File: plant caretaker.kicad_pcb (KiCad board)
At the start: 2 copper layers, 56 parts, among them J3 Water_Pump, J4 Kitronik, J5 694106402002, Q1 FDMS86255, U1 UDA1380HN_N2, U2 TMP175AIDR, U4 LM2596S-5, U5 PAM8403D, U6 ESP32_C3_ZERO

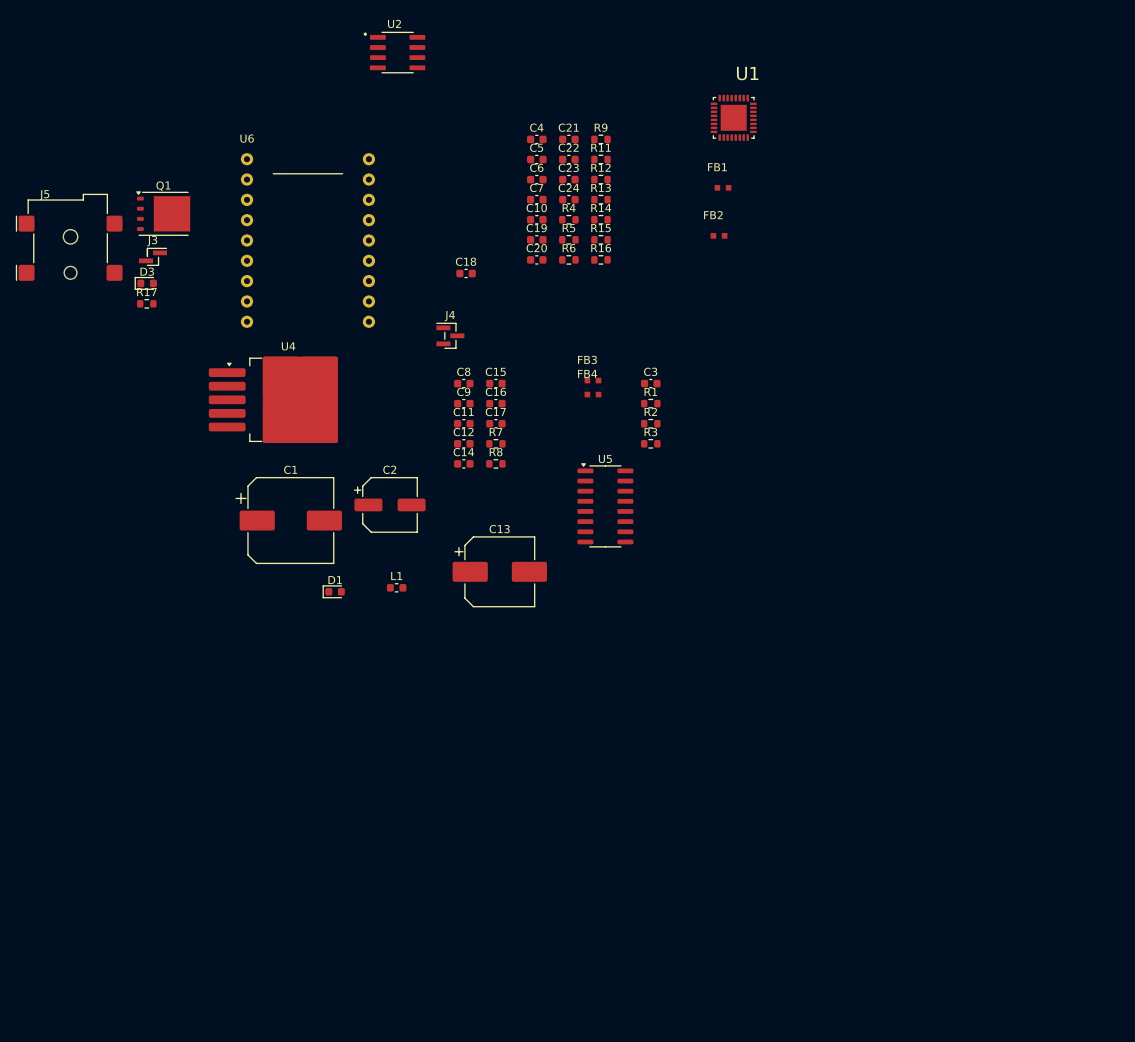
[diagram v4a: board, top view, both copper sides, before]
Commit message: Started power connections
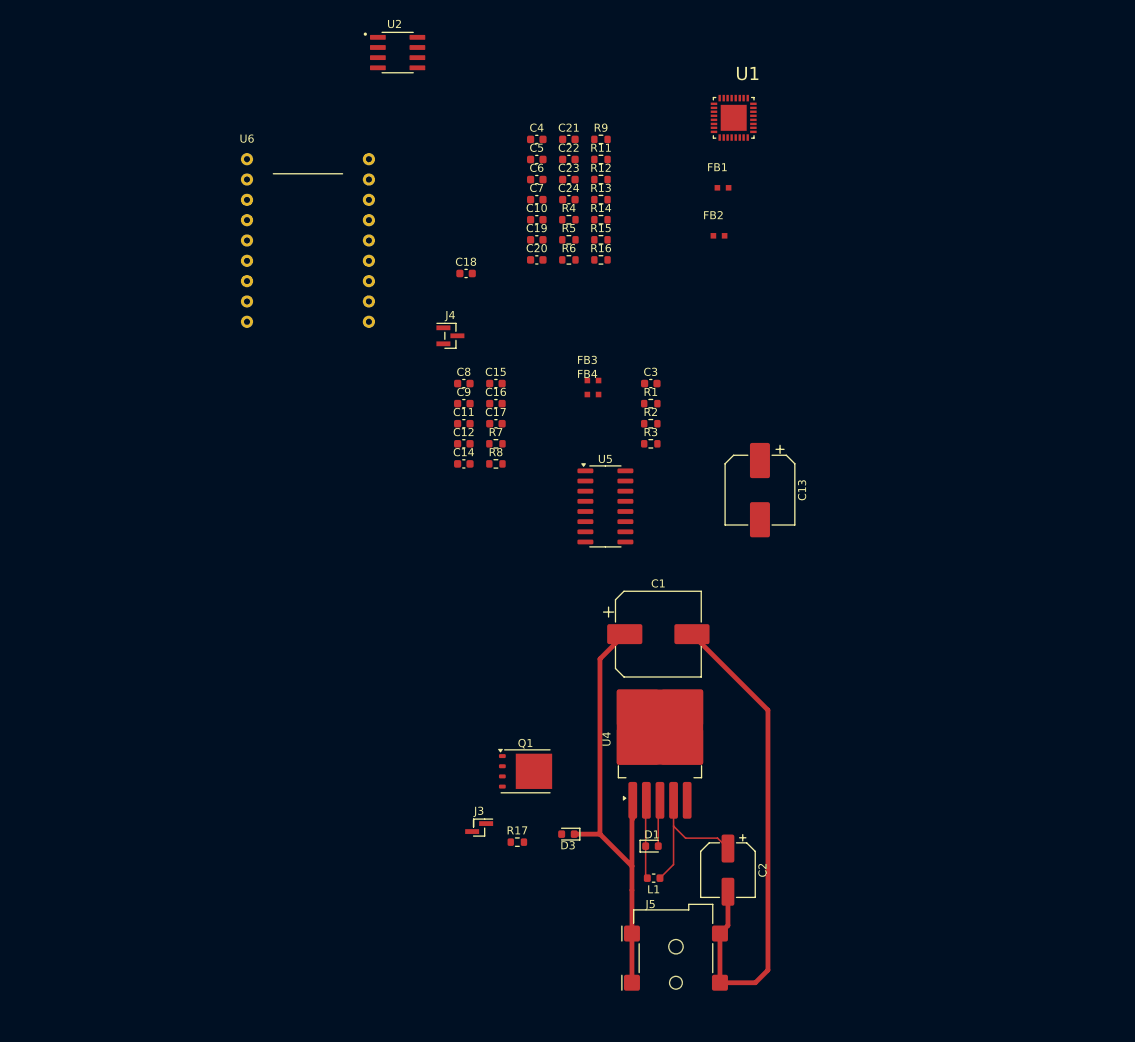
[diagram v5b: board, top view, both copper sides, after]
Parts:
- moved J5 116.6 mm to (118.0, 133.0)
- moved D3 86.6 mm to (104.5, 117.5), turned to 180 degrees
- moved Q1 83.1 mm to (99.2, 109.7)
- moved J3 82.2 mm to (93.4, 116.7)
- moved R17 81.7 mm to (98.2, 118.5)
- moved U4 62.9 mm to (116.0, 105.6), turned to 90 degrees
- moved C2 62.2 mm to (124.5, 122.0), turned to -90 degrees
- moved D1 50.8 mm to (115.0, 119.0)
- moved L1 48.5 mm to (115.2, 123.0), turned to 180 degrees
- moved C1 48.1 mm to (115.8, 92.5)
- moved C13 34.1 mm to (128.5, 74.5), turned to -90 degrees
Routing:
- net GND: track 0.00 -> 70.2 mm
- net Net-(D3-K): track 0.00 -> 60.3 mm
- net /BuckConverter/5V_OUT: track 0.00 -> 18.4 mm
- net Net-(D1-K): track 0.00 -> 9.85 mm

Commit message: Added power polygon and edge cuts
Also added 12V label to schematic for polygon net class
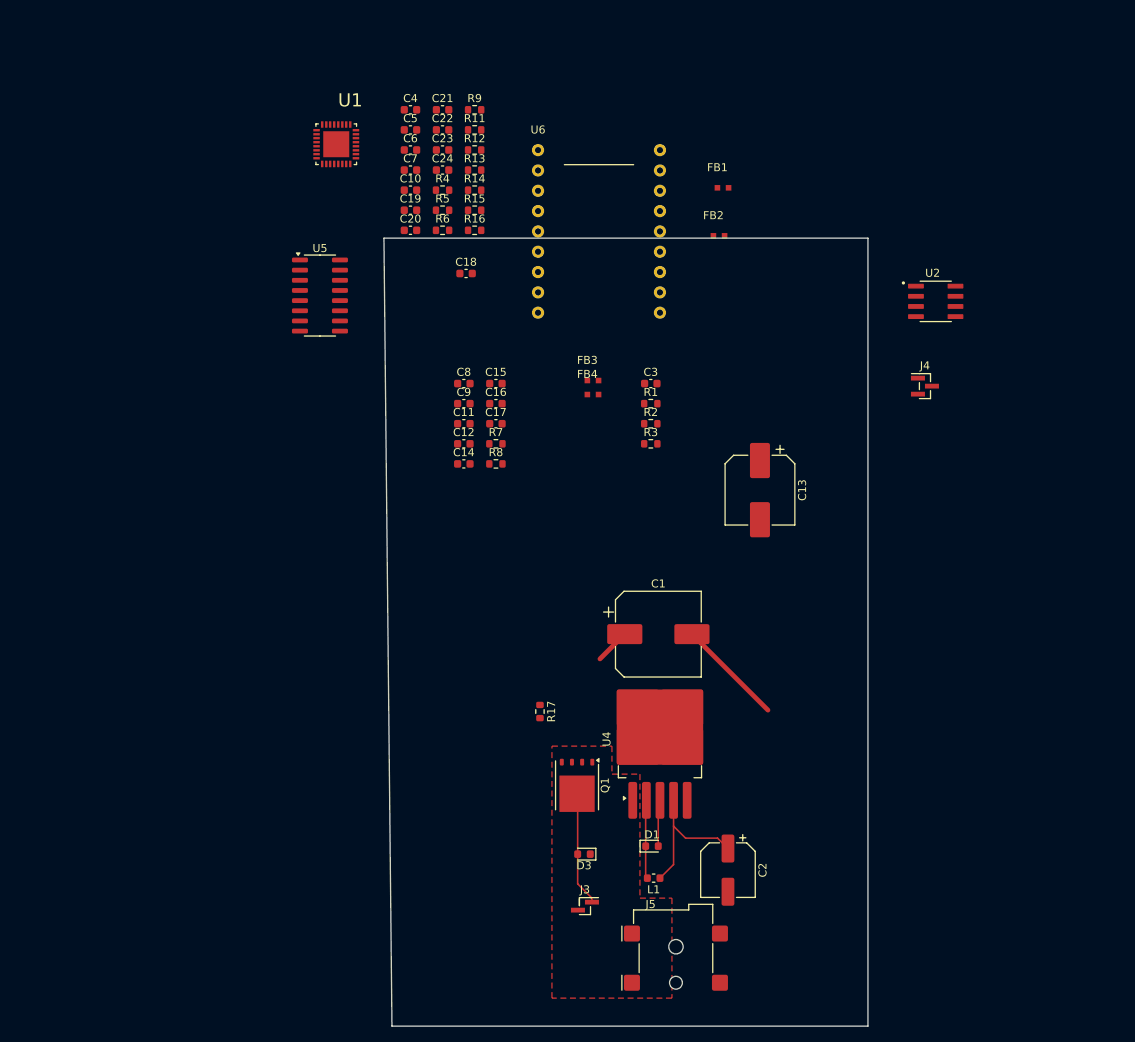
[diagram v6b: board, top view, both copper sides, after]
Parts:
- moved U2 74.1 mm to (150.5, 50.9)
- moved J4 59.7 mm to (149.1, 61.5)
- moved U1 49.8 mm to (75.5, 31.3)
- moved U5 44.4 mm to (73.5, 50.2)
- moved U6 36.4 mm to (100.8, 32.0)
- moved R17 16.6 mm to (101.0, 102.2), turned to -90 degrees
- moved J3 16.5 mm to (106.6, 126.5)
- moved C10 16.2 mm to (84.8, 37.0)
- moved C19 16.2 mm to (84.8, 39.5)
- moved C20 16.2 mm to (84.8, 42.0)
- moved C4 16.2 mm to (84.8, 27.0)
- moved C5 16.2 mm to (84.8, 29.5)
- moved C6 16.2 mm to (84.8, 32.0)
- moved C7 16.2 mm to (84.8, 34.5)
- moved R11 16.2 mm to (92.8, 29.5)
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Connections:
- net Net-(D3-K) renamed /BuckConverter/12V
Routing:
- net /BuckConverter/12V: track 60.3 -> 4.38 mm
- net GND: track 70.2 -> 19.2 mm
- net Net-(D3-A): track 0.00 -> 14.3 mm
- added copper zone on F.Cu, net /BuckConverter/12V
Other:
- board outline added: 60.5 x 98.5 mm

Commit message: PCB - power connected
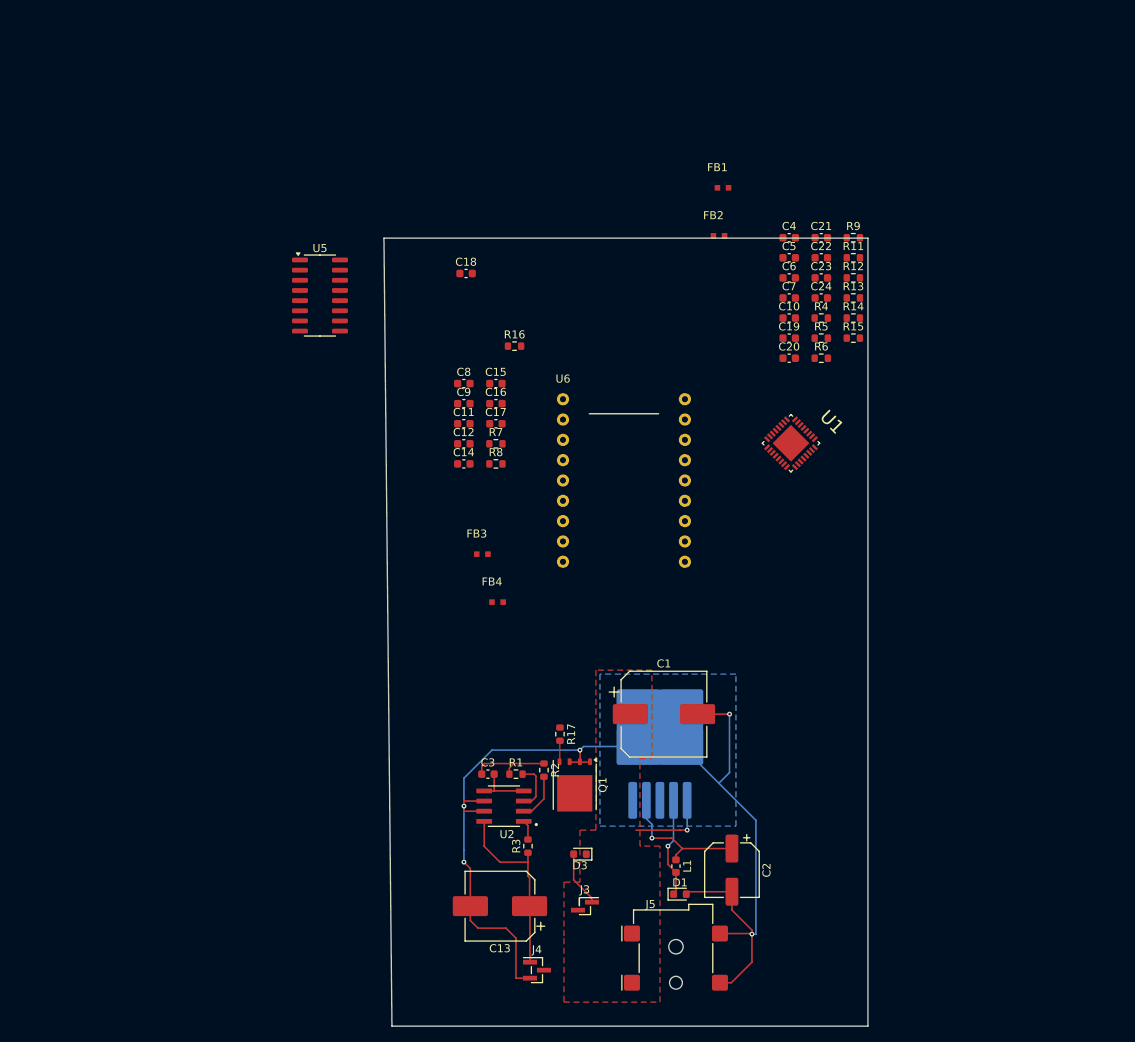
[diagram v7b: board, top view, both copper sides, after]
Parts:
- U4: moved to B.Cu
- moved J4 87.6 mm to (100.6, 134.5)
- moved U2 83.0 mm to (96.5, 114.0), turned to 180 degrees
- moved U1 68.0 mm to (132.4, 68.6), turned to -45 degrees
- moved C13 61.3 mm to (96.0, 126.5), turned to 180 degrees
- moved C3 52.9 mm to (94.5, 110.0)
- moved R3 52.6 mm to (99.5, 119.0), turned to 90 degrees
- moved R11 50.0 mm to (140.2, 45.5)
- moved R12 50.0 mm to (140.2, 48.0)
- moved R13 50.0 mm to (140.2, 50.5)
- moved R14 50.0 mm to (140.2, 53.0)
- moved R15 50.0 mm to (140.2, 55.5)
- moved R9 50.0 mm to (140.2, 43.0)
- moved C10 50.0 mm to (132.2, 53.0)
- moved C19 50.0 mm to (132.2, 55.5)
- moved C20 50.0 mm to (132.2, 58.0)
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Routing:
- net GND: track 19.2 -> 138.0 mm, vias 0 -> 5
- net +3V3: track 0.00 -> 33.7 mm
- net Net-(D3-A): track 14.3 -> 6.95 mm
- net /TempSensor/ALERT: track 0.00 -> 6.10 mm
- net /AudioCodec/SCL: track 0.00 -> 5.93 mm
- net /BuckConverter/12V: track 4.38 -> 10.2 mm, vias 0 -> 1
- net Net-(D1-K): track 9.85 -> 12.5 mm, vias 0 -> 1
- net Net-(Q1-G): track 0.00 -> 2.68 mm
- net /AudioCodec/SDA: track 0.00 -> 2.49 mm
- net /BuckConverter/5V_OUT: track 18.4 -> 16.8 mm, vias 0 -> 1
- added copper zone on B.Cu, net GND

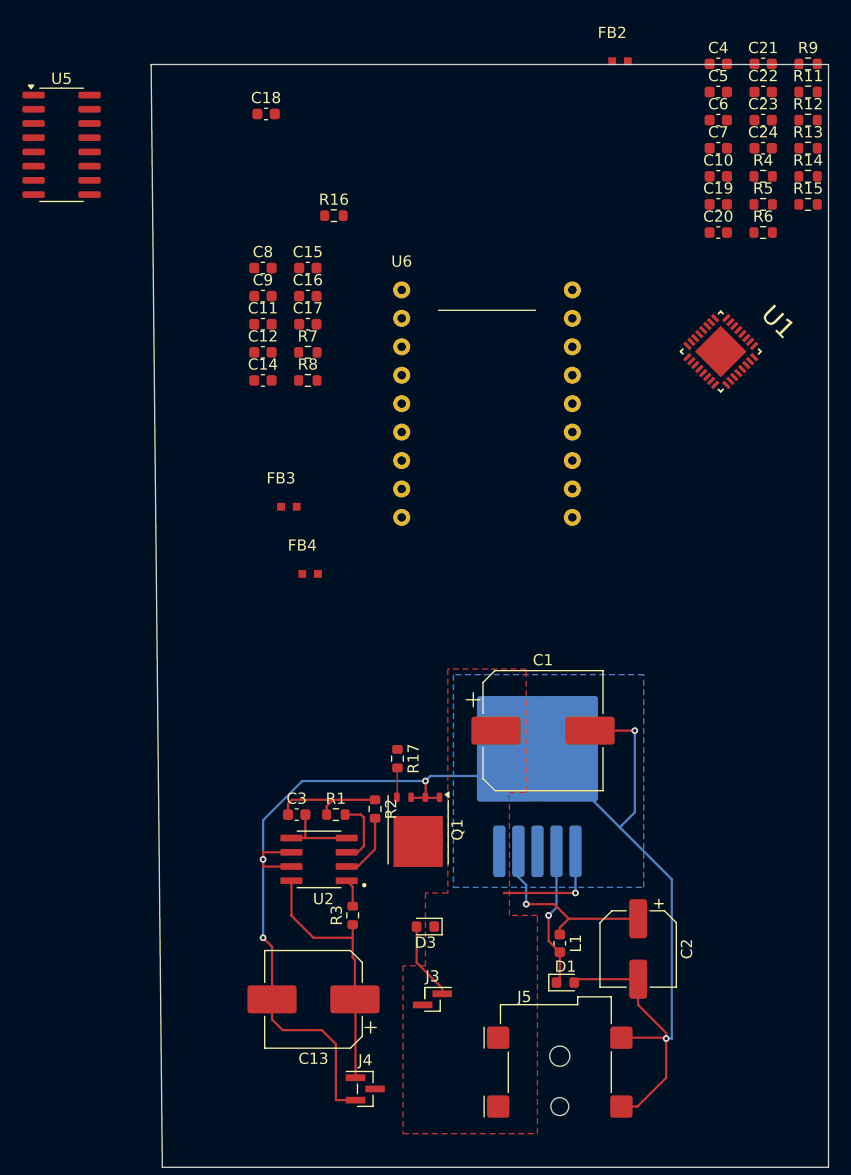
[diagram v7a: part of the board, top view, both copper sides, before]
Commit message: Fixed ESP32 library
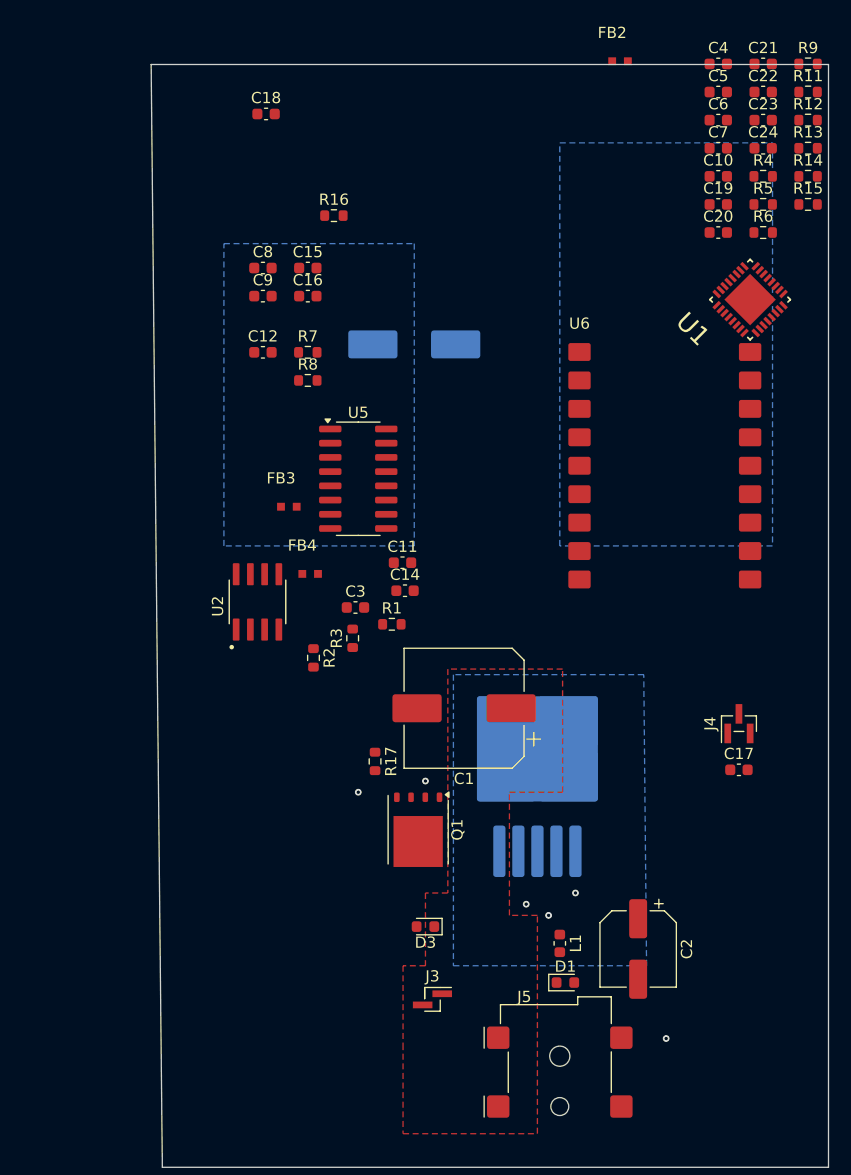
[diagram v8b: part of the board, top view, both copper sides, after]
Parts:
- C13: moved to B.Cu
- U6: footprint ESP32_C3_ZERO_Library:ESP32_C3_ZERO -> ESP32_C3_Zero:ESP32_C3_ZERO
- moved C13 59.2 mm to (105.0, 68.0)
- moved C17 55.4 mm to (134.0, 106.0)
- moved J4 46.7 mm to (134.0, 101.9), turned to 90 degrees
- moved U5 39.9 mm to (100.0, 80.0)
- moved R3 24.8 mm to (99.5, 94.2)
- moved C11 24.7 mm to (104.0, 87.5)
- moved U2 23.6 mm to (91.0, 91.0), turned to 90 degrees
- moved C14 22.7 mm to (104.2, 90.0)
- moved C3 19.2 mm to (99.8, 91.5)
- moved R1 17.7 mm to (103.0, 93.0)
- moved U6 16.8 mm to (119.8, 68.7)
- moved R2 14.6 mm to (96.0, 96.0)
- moved C1 7.33 mm to (109.5, 100.5), turned to 180 degrees
- moved U1 5.33 mm to (135.0, 64.0), turned to 135 degrees
- moved R17 2.02 mm to (101.5, 105.2)
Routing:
- net GND: track 138.0 -> 0.13 mm, vias 5 -> 3
- net +3V3: track 33.7 -> 0.00 mm
- net /BuckConverter/5V_OUT: track 16.8 -> 0.00 mm
- net Net-(D1-K): track 12.5 -> 0.00 mm
- net /BuckConverter/12V: track 10.2 -> 0.04 mm
- net Net-(D3-A): track 6.95 -> 0.00 mm
- net /TempSensor/ALERT: track 6.10 -> 0.00 mm
- net /AudioCodec/SCL: track 5.93 -> 0.00 mm
- net Net-(Q1-G): track 2.68 -> 0.00 mm
- net /AudioCodec/SDA: track 2.49 -> 0.00 mm
